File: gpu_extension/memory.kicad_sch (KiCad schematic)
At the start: 6 parts

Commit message: schematic for gpu extension
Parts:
- removed C: C, symbol Device:C
- removed R: R, symbol Device:R
- removed U: ESP-PSRAM32, Package_SO:SOIC-8_3.9x4.9mm_P1.27mm, symbol Memory_RAM:ESP-PSRAM32
- added C403: 100n, Capacitor_SMD:C_0603_1608Metric_Pad1.08x0.95mm_HandSolder, symbol Device:C
- added C404: 1u, Capacitor_SMD:C_0603_1608Metric_Pad1.08x0.95mm_HandSolder, symbol Device:C
- added R403: 10k, Resistor_SMD:R_0603_1608Metric_Pad0.98x0.95mm_HandSolder, symbol Device:R
- added U3: APS6408L-3OBM-BA, BGA24C100P5X5_600X800X120, symbol APS6408L-3OBM-BA:APS6408L-3OBM-BA
- C401: renamed from C; value C -> 100n; footprint (none) -> Capacitor_SMD:C_0603_1608Metric_Pad1.08x0.95mm_HandSolder
- R401: renamed from R; value R -> 10k; footprint (none) -> Resistor_SMD:R_0603_1608Metric_Pad0.98x0.95mm_HandSolder
- renumbered U to U401
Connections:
- net +3V3: now also C403.1, C404.1, R403.1, U3.B4 (VDD), U3.D1 (VDDQ), U3.E4 (VDDQ)
- net GND: now also C403.2, C404.2, U3.B3 (VSS), U3.C1 (VSSQ), U3.E5 (VSSQ)
- new net: U3.A2 (NC), U3.A5 (NC), U3.B1 (NC), U3.B5 (NC), U3.C5 (NC)
- new net PSRAM.CE#: R403.2, U3.A3 (~{CE})
- new net PSRAM.IO0: U3.D3 (ADQ0)
- new net PSRAM.IO1: U3.D2 (ADQ1)
- new net PSRAM.IO2: U3.C4 (ADQ2)
- new net PSRAM.IO3: U3.D4 (ADQ3)
- new net PSRAM.IO4: U3.D5 (ADQ4)
- new net PSRAM.IO5: U3.E3 (ADQ5)
- new net PSRAM.IO6: U3.E2 (ADQ6)
- new net PSRAM.IO7: U3.E1 (ADQ7)
- new net PSRAM.RWDS: U3.C3 (DQS/DM)
- no-connect marks 0 -> 2

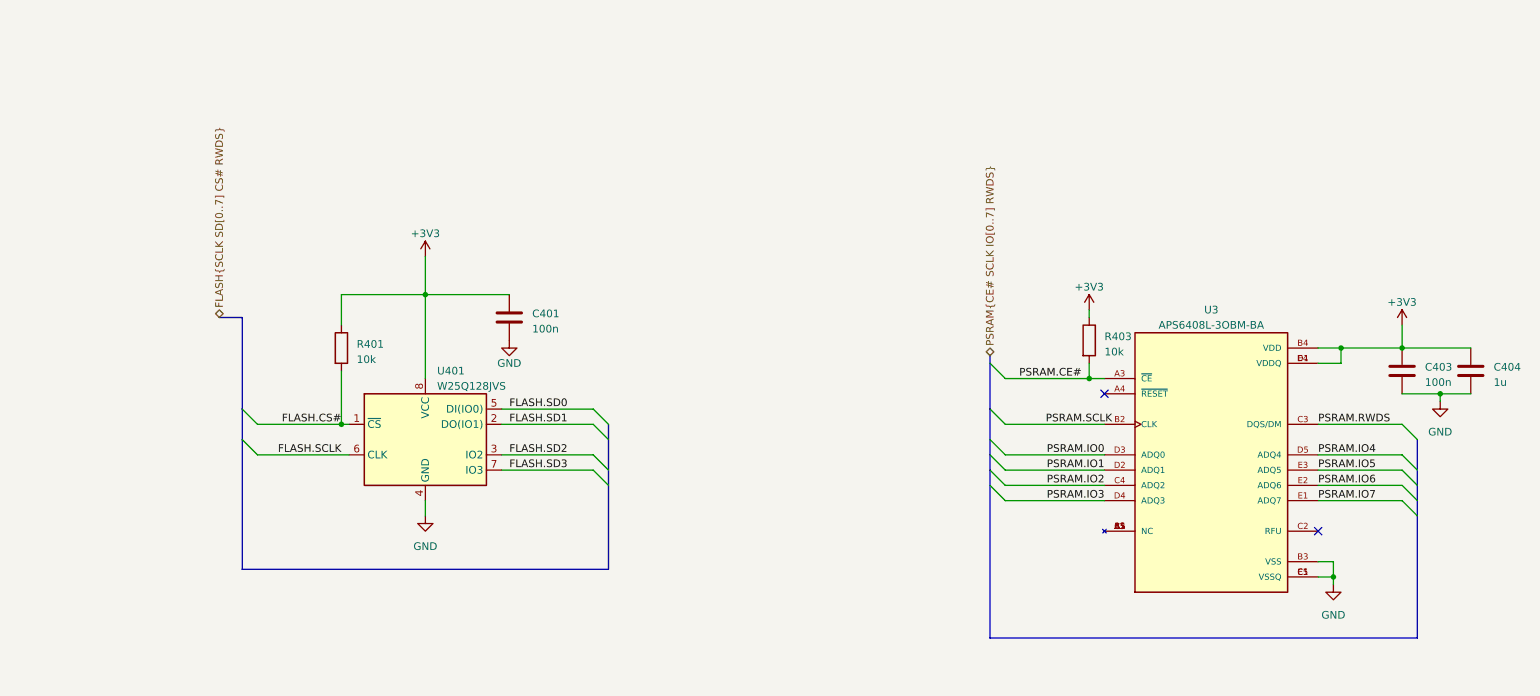
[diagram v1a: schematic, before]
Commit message: some ERC fixes
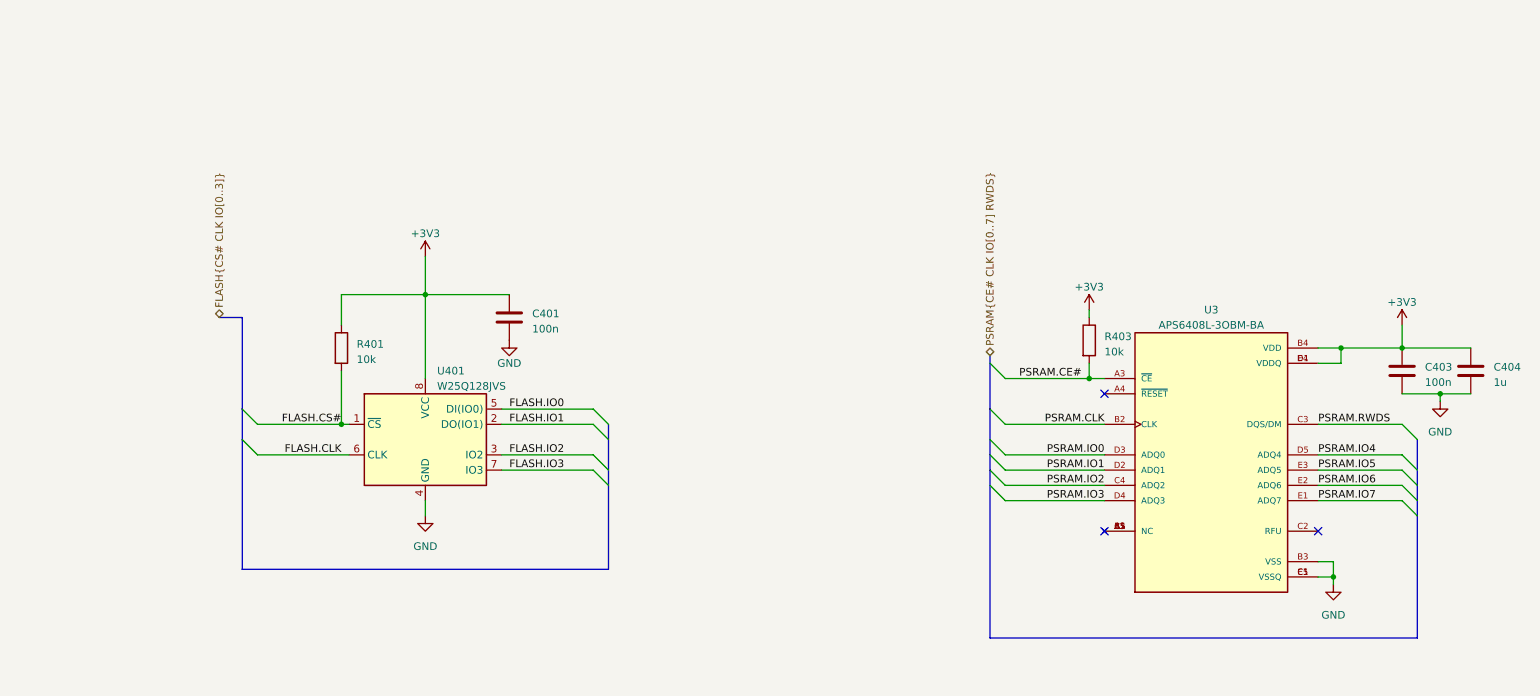
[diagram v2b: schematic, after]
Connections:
- net PSRAM.CLK: now reaches U3.B2 (CLK)
- net FLASH.SCLK renamed FLASH.CLK
- net FLASH.SD0 renamed FLASH.IO0
- net FLASH.SD1 renamed FLASH.IO1
- net FLASH.SD2 renamed FLASH.IO2
- net FLASH.SD3 renamed FLASH.IO3
- no-connect marks 2 -> 3
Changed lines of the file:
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@@
   )
   (no_connect (at 227.33 107.95))
+  (no_connect (at 191.77 107.95))
   (no_connect (at 191.77 85.09))
   (bus_entry (at 172.72 87.63) (size 2.54 2.54)
@@
     (effects (font (size 1.27 1.27)) (justify right bottom))
   )
-  (label "FLASH.SD3" (at 92.71 97.79 0) (fields_autoplaced)
+  (label "FLASH.IO3" (at 92.71 97.79 0) (fields_autoplaced)
     (effects (font (size 1.27 1.27)) (justify left bottom))
   )
@@
     (effects (font (size 1.27 1.27)) (justify left bottom))
   )
-  (label "FLASH.SD1" (at 92.71 90.17 0) (fields_autoplaced)
-    (effects (font (size 1.27 1.27)) (justify left bottom))
-  )
-  (label "PSRAM.SCLK" (at 193.04 90.17 180) (fields_autoplaced)
+  (label "FLASH.IO1" (at 92.71 90.17 0) (fields_autoplaced)
+    (effects (font (size 1.27 1.27)) (justify left bottom))
+  )
+  (label "PSRAM.CLK" (at 191.77 90.17 180) (fields_autoplaced)
     (effects (font (size 1.27 1.27)) (justify right bottom))
   )
@@
     (effects (font (size 1.27 1.27)) (justify left bottom))
   )
-  (label "FLASH.SD0" (at 92.71 87.63 0) (fields_autoplaced)
-    (effects (font (size 1.27 1.27)) (justify left bottom))
-  )
-  (label "FLASH.SD2" (at 92.71 95.25 0) (fields_autoplaced)
+  (label "FLASH.IO0" (at 92.71 87.63 0) (fields_autoplaced)
+    (effects (font (size 1.27 1.27)) (justify left bottom))
+  )
+  (label "FLASH.IO2" (at 92.71 95.25 0) (fields_autoplaced)
     (effects (font (size 1.27 1.27)) (justify left bottom))
   )
@@
     (effects (font (size 1.27 1.27)) (justify right bottom))
   )
-  (label "FLASH.SCLK" (at 64.77 95.25 0) (fields_autoplaced)
-    (effects (font (size 1.27 1.27)) (justify right bottom))
-  )
-  (hierarchical_label "FLASH{SCLK SD[0..7] CS# RWDS}" (shape bidirectional) (at 44.45 72.39 90) (fields_autoplaced)
+  (label "FLASH.CLK" (at 64.77 95.25 0) (fields_autoplaced)
+    (effects (font (size 1.27 1.27)) (justify right bottom))
+  )
+  (hierarchical_label "FLASH{CS# CLK IO[0..3]}" (shape bidirectional) (at 44.45 72.39 90) (fields_autoplaced)
     (effects (font (size 1.27 1.27)) (justify left))
   )
-  (hierarchical_label "PSRAM{CE# SCLK IO[0..7] RWDS}" (shape bidirectional) (at 172.72 78.74 90) (fields_autoplaced)
+  (hierarchical_label "PSRAM{CE# CLK IO[0..7] RWDS}" (shape bidirectional) (at 172.72 78.74 90) (fields_autoplaced)
     (effects (font (size 1.27 1.27)) (justify left))
   )

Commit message: gpu and motherboard passes tests, now time for fpga
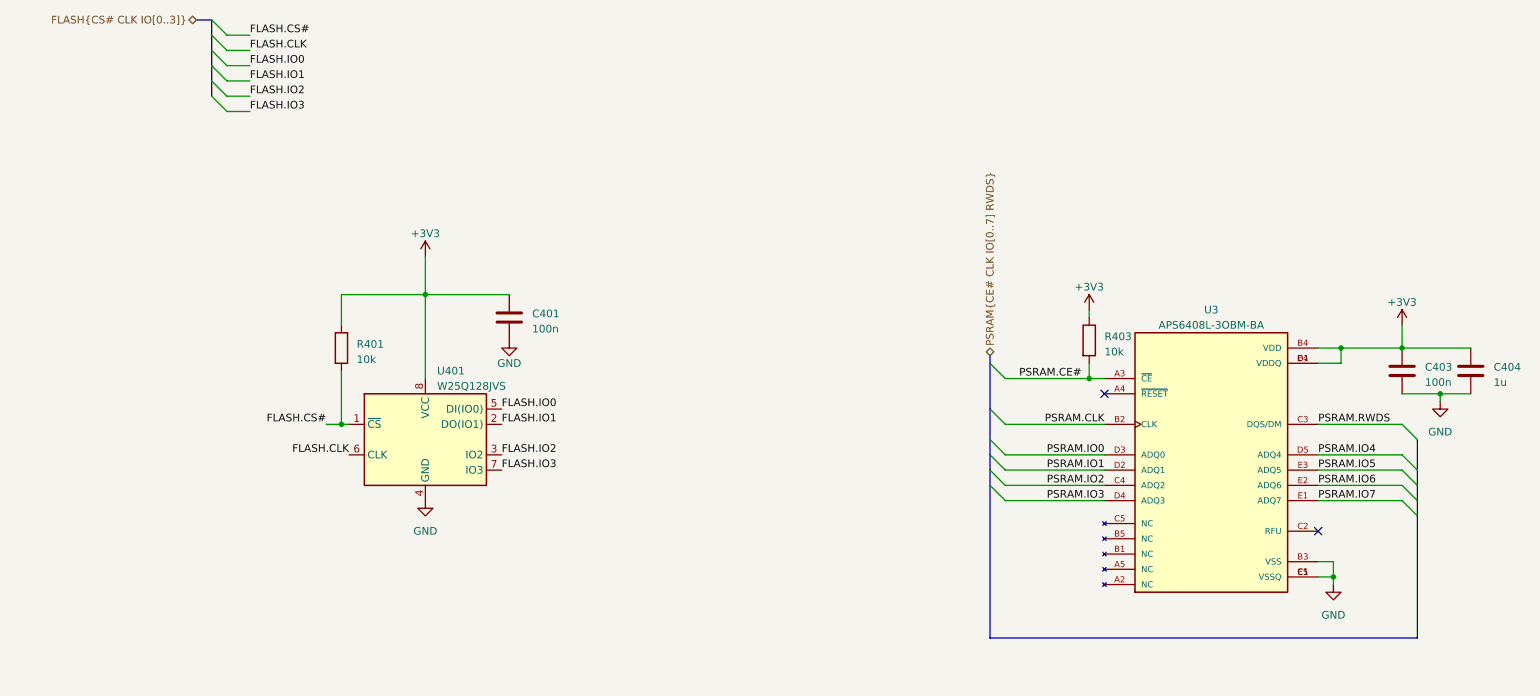
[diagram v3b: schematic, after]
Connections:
- now unconnected: U3.A2 (NC), U3.A5 (NC), U3.B1 (NC), U3.B5 (NC), U3.C5 (NC)
- no-connect marks 3 -> 2

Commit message: fixes in gpu extension schematic
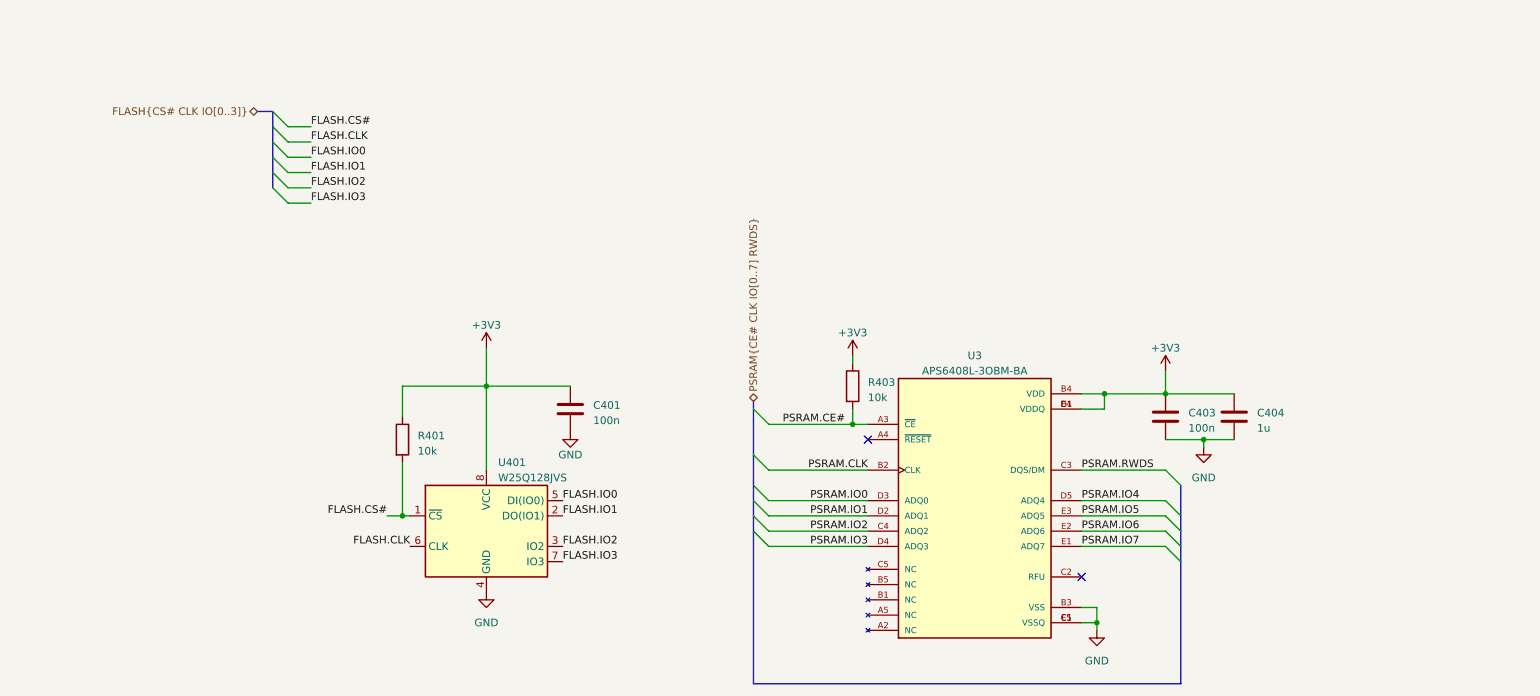
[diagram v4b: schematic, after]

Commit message: fixes
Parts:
- removed C401, C403: 100n, Capacitor_SMD:C_0603_1608Metric_Pad1.08x0.95mm_HandSolder, symbol Device:C
- removed R401, R403: 10k, Resistor_SMD:R_0603_1608Metric_Pad0.98x0.95mm_HandSolder, symbol Device:R
- removed U3: APS6408L-3OBM-BA, BGA24C100P5X5_600X800X120, symbol APS6408L-3OBM-BA:APS6408L-3OBM-BA
- removed U401: W25Q128JVS, Package_SO:SOIC-8_5.23x5.23mm_P1.27mm, symbol Memory_Flash:W25Q128JVS
- added R404, R406: 10k, Resistor_SMD:R_0402_1005Metric_Pad0.72x0.64mm_HandSolder, symbol Device:R
- added U1: GD25D05CT, Package_SO:SOP-8_3.9x4.9mm_P1.27mm, symbol Memory_Flash:GD25D05CT
- C404: value 1u -> 100n; footprint Capacitor_SMD:C_0603_1608Metric_Pad1.08x0.95mm_HandSolder -> Capacitor_SMD:C_0402_1005Metric_Pad0.74x0.62mm_HandSolder
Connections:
- net +3V3: now also R404.1, R406.1, U1.8 (VCC)
- net FLASH.CLK: now also U1.6 (SCLK)
- net FLASH.CS#: now also R406.2, U1.1 (~{CS})
- net FLASH.IO0: now also U1.5 (SI/IO0)
- net FLASH.IO1: now also U1.2 (O1/SO)
- net GND: now also U1.4 (VSS)
- new net: R404.2, U1.3 (~{WP})
- no-connect marks 2 -> 0

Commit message: version 1.0
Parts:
- removed R406: 10k, Resistor_SMD:R_0402_1005Metric_Pad0.72x0.64mm_HandSolder, symbol Device:R
- removed U1: GD25D05CT, Package_SO:SOP-8_3.9x4.9mm_P1.27mm, symbol Memory_Flash:GD25D05CT
- added U1: W25Q32JVSS, Package_SO:SOIC-8_5.23x5.23mm_P1.27mm, symbol Memory_Flash:W25Q32JVSS
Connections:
- net +3V3: now also U1.8 (VCC)
- net FLASH.CLK: now also U1.6 (CLK)
- net FLASH.CS#: now also R404.2, U1.1 (~{CS})
- net FLASH.IO0: now also U1.5 (DI(IO0))
- net FLASH.IO1: now also U1.2 (DO(IO1))
- net GND: now also U1.4 (GND)
- new net FLASH.IO2: U1.3 (IO2)
- new net FLASH.IO3: U1.7 (IO3)

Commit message: prepared first versions of PCBs
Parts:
- renumbered C404 to C1, R404 to R28
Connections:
- net FLASH.CLK renamed QSPI.CLK
- net FLASH.CS# renamed QSPI.CS#
- net FLASH.IO0 renamed QSPI.IO0
- net FLASH.IO1 renamed QSPI.IO1
- net FLASH.IO2 renamed QSPI.IO2
- net FLASH.IO3 renamed QSPI.IO3
